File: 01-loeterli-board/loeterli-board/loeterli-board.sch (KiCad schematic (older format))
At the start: 76 parts, among them J1 RPC1-12RB-6P, J2 Conn_01x01, J3 Conn_01x04, J5 Screw_Terminal_01x03, Q1 PSMN5R2-60YL, SW1 SW_Push, SW2 SW_Push, SW3 SW_Push, SW4 SW_Push, U1 VOM1271T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

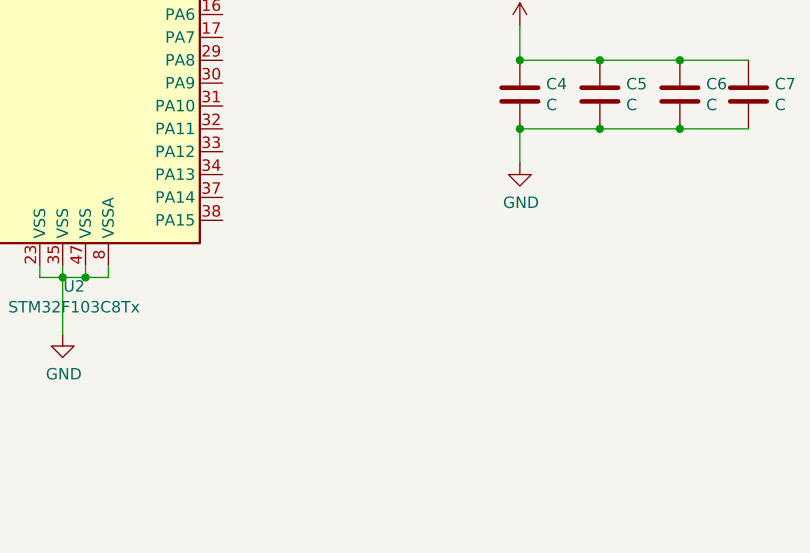
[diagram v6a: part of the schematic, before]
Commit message: SWD connector
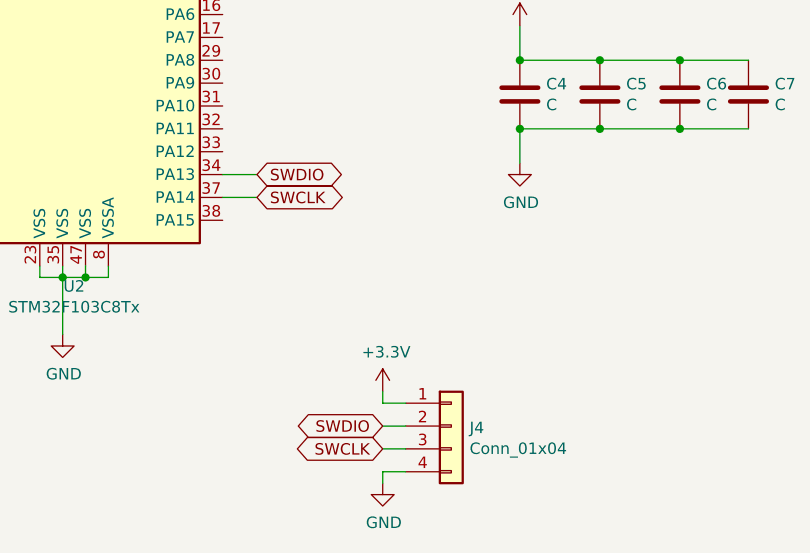
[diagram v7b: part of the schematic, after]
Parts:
- added J4: Conn_01x04, symbol Connector_Generic:Conn_01x04
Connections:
- net +3V3: now also J4.1 (Pin_1)
- net GND: now also J4.4 (Pin_4)
- net SWDIO: now reaches U2.34 (PA13)
- net SWDIO: now also J4.2 (Pin_2)
- net SWCLK: now reaches U2.37 (PA14)
- net SWCLK: now also J4.3 (Pin_3)
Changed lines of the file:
@@
 EESchema Schematic File Version 4
 LIBS:loeterli-board-cache
-EELAYER 29 0
+EELAYER 30 0
 EELAYER END
 $Descr A4 11693 8268
@@
 	1    0    0    -1
 $EndComp
-$Comp
-L MCU_ST_STM32F1:STM32F103C8Tx U2
-U 1 1 5ECEDED5
-P 4650 4950
-F 0 "U2" H 4600 3361 50  0000 C CNN
-F 1 "STM32F103C8Tx" H 4600 3270 50  0000 C CNN
-F 2 "Package_QFP:LQFP-48_7x7mm_P0.5mm" H 4050 3550 50  0001 R CNN
-F 3 "http://www.st.com/st-web-ui/static/active/en/resource/technical/document/datasheet/CD00161566.pdf" H 4650 4950 50  0001 C CNN
-	1    4650 4950
-	1    0    0    -1
-$EndComp
 Connection ~ 9050 3050
 Wire Wire Line
@@
 Wire Wire Line
 	10100 6150 10000 6150
+Text GLabel 5400 6150 2    50   BiDi ~ 0
+SWCLK
+Wire Wire Line
+	5250 6050 5400 6050
+Text GLabel 5400 6050 2    50   BiDi ~ 0
+SWDIO
+Wire Wire Line
+	5400 6150 5250 6150
+Wire Wire Line
+	5950 7350 6050 7350
+Wire Wire Line
+	5950 7400 5950 7350
+Wire Wire Line
+	5950 7050 5950 7000
+Wire Wire Line
+	6050 7050 5950 7050
+$Comp
+L power:+3.3V #PWR01
+U 1 1 5ED869B1
+P 5950 7000
+F 0 "#PWR01" H 5950 6850 50  0001 C CNN
+F 1 "+3.3V" H 5965 7173 50  0000 C CNN
+F 2 "" H 5950 7000 50  0001 C CNN
+F 3 "" H 5950 7000 50  0001 C CNN
+	1    5950 7000
+	1    0    0    -1
+$EndComp
+$Comp
+L power:GND #PWR02
+U 1 1 5ED84EDE
+P 5950 7400
+F 0 "#PWR02" H 5950 7150 50  0001 C CNN
+F 1 "GND" H 5955 7227 50  0000 C CNN
+F 2 "" H 5950 7400 50  0001 C CNN
+F 3 "" H 5950 7400 50  0001 C CNN
+	1    5950 7400
+	1    0    0    -1
+$EndComp
+Text GLabel 5950 7250 0    50   BiDi ~ 0
+SWCLK
+Wire Wire Line
+	5950 7250 6050 7250
+Text GLabel 5950 7150 0    50   BiDi ~ 0
+SWDIO
+Wire Wire Line
+	6050 7150 5950 7150
+$Comp
+L Connector_Generic:Conn_01x04 J4
+U 1 1 5ED1936A
+P 6250 7150
+F 0 "J4" H 6330 7142 50  0000 L CNN
+F 1 "Conn_01x04" H 6330 7051 50  0000 L CNN
+F 2 "" H 6250 7150 50  0001 C CNN
+F 3 "~" H 6250 7150 50  0001 C CNN
+	1    6250 7150
+	1    0    0    -1
+$EndComp
+$Comp
+L MCU_ST_STM32F1:STM32F103C8Tx U2
+U 1 1 5ECEDED5
+P 4650 4950
+F 0 "U2" H 4600 3361 50  0000 C CNN
+F 1 "STM32F103C8Tx" H 4600 3270 50  0000 C CNN
+F 2 "Package_QFP:LQFP-48_7x7mm_P0.5mm" H 4050 3550 50  0001 R CNN
+F 3 "http://www.st.com/st-web-ui/static/active/en/resource/technical/document/datasheet/CD00161566.pdf" H 4650 4950 50  0001 C CNN
+	1    4650 4950
+	1    0    0    -1
+$EndComp
 $EndSCHEMATC

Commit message: pinbelegung etc
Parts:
- removed J4: Conn_01x04, symbol Connector_Generic:Conn_01x04
- added C19, C20, C21, C22, C23: C, Capacitor_SMD:C_1206_3216Metric, symbol Device:C
- added C24: C, Capacitor_SMD:C_0603_1608Metric, symbol Device:C
- added D1: SP0502BAHT, Package_TO_SOT_SMD:SOT-23, symbol Power_Protection:SP0502BAHT
- added R30, R31, R32, R33, R34, R35, R36, R37, R38, R39, R40, R41, R42: R, Resistor_SMD:R_0603_1608Metric, symbol Device:R
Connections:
- net +3V3: now also J3.1 (Pin_1), R33.1, R34.1, R35.1, R36.1, R37.1, R41.2
- net GND: now also J3.4 (Pin_4), SW2.1, SW3.1, SW4.1, C19.2, C20.2, C21.2, C22.2, C23.2, C24.2, D1.3 (A), R40.2
- net SWCLK: now also J3.3 (Pin_3)
- net SWDIO: now also J3.2 (Pin_2)
- net TEMP: now also U2.10 (PA0)
- net V_RECT: now also R39.1
- net ZCD: now also U2.42 (PB6)
- net nGATE: now also U2.13 (PA3)
- net SLEEP_EXT: now reaches J1.6
- net SLEEP_EXT: now also U2.45 (PB8)
- net LED_ZZZ: now reaches D8.1 (K)
- net LED_ZZZ: now also U2.41 (PB5)
- net at D8.2 (A): now also R36.2
- net LED_RDY: now reaches D9.1 (K)
- net LED_RDY: now also U2.32 (PA11)
- net at D9.2 (A): now also R37.2
- net V_RECT_SENSE: now reaches U2.11 (PA1)
- net V_RECT_SENSE: now also C22.1, R39.2, R40.1
- net I_SENSE: now reaches U2.12 (PA2)
- net I_SENSE: now also C24.1, R42.2
- net DIG2_B: now reaches U2.15 (PA5)
- net DIG2_B: now also R27.1
- net DIG2_A: now reaches U2.16 (PA6)
- net DIG2_A: now also R23.1
- net DIG2_F: now reaches U2.17 (PA7)
- net DIG2_F: now also R29.1
- net DIG1_B: now reaches U2.18 (PB0)
- net DIG1_B: now also R16.1
- net DIG1_A: now reaches U2.19 (PB1)
- net DIG1_A: now also R19.1
- net DIG1_G: now reaches U2.21 (PB10)
- net DIG1_G: now also R22.1
- net DIG1_F: now reaches U2.22 (PB11)
- net DIG1_F: now also R18.1
- net DIG1_E: now reaches U2.25 (PB12)
- net DIG1_E: now also R21.1
- net DIG1_D: now reaches U2.26 (PB13)
- net DIG1_D: now also R17.1
- net DIG1_C: now reaches U2.27 (PB14)
- net DIG1_C: now also R20.1
- net DIG2_E: now reaches U2.28 (PB15)
- net DIG2_E: now also R25.1
- net DIG2_D: now reaches U2.29 (PA8)
- net DIG2_D: now also R28.1
- net DIG2_G: now reaches U2.30 (PA9)
- net DIG2_G: now also R26.1
- net DIG2_C: now reaches U2.31 (PA10)
- net DIG2_C: now also R24.1
- net SW_DOWN: now reaches U2.33 (PA12)
- net SW_DOWN: now also C20.1, R31.1, R34.2
- net SW_UP: now reaches U2.39 (PB3)
- net SW_UP: now also C19.1, R30.1, R33.2
- net SW_ZZZ: now reaches U2.40 (PB4)
- net SW_ZZZ: now also C21.1, R32.1, R35.2
- net at U2.46 (PB9): now also C23.1, D1.1 (K), R38.1, R41.1
- net SLEEP_MOUNT: now reaches J2.1 (Pin_1)
- net SLEEP_MOUNT: now also R38.2
- net at U4.6: now also R42.1
- net at SW2.2: now also R31.2
- net at SW3.2: now also R32.2
- net at SW4.2: now also R30.2
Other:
- moved on the sheet: C4, C5, C6, C7, D8, D9, F2, J1, J2, J3, SW2, SW3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
